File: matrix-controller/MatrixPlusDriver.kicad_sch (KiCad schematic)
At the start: 2 parts, among them IC1 IS31FL3728-QFLS2-TR, U1 1088BS

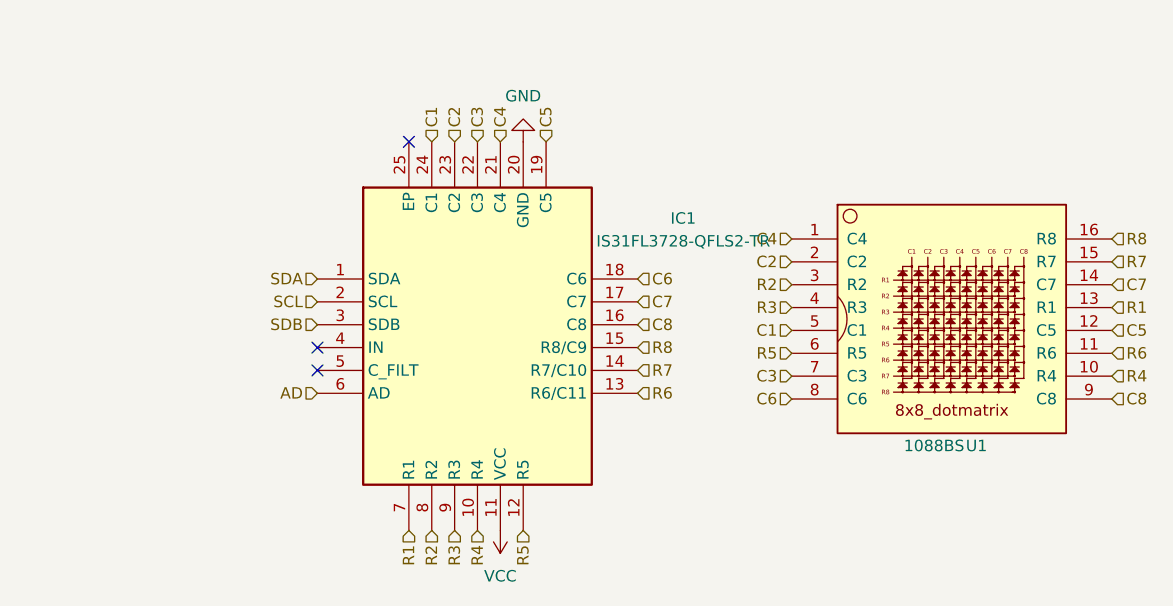
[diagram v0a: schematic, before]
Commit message: Schematic of other pannels mostly completed
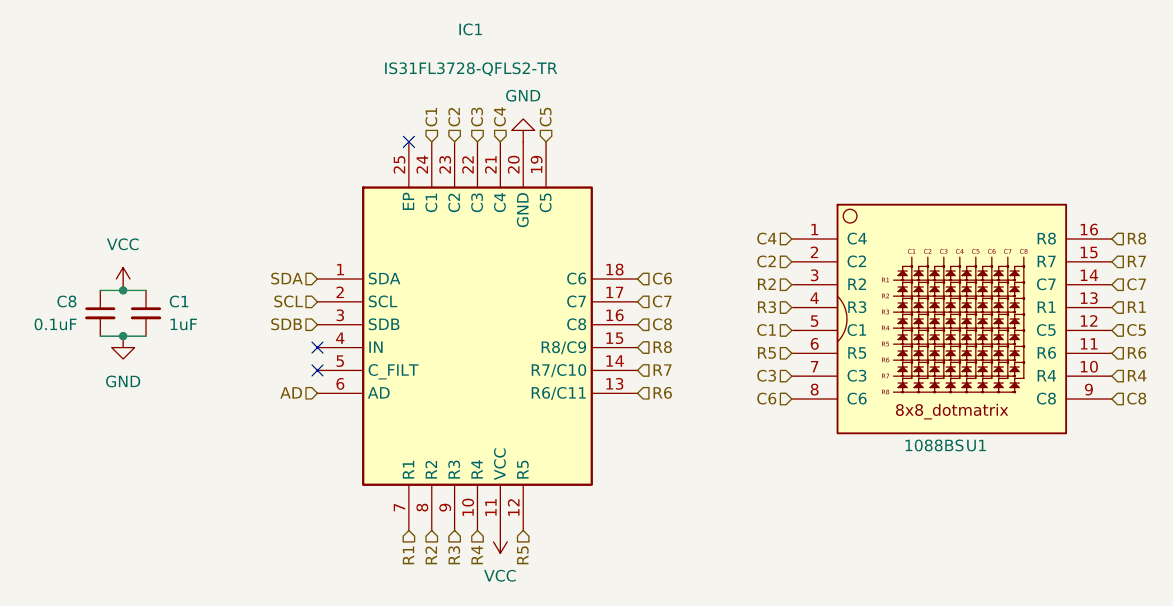
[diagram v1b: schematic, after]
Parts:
- added C1: 1uF, symbol Device:C_Small
- added C8: 0.1uF, symbol Device:C_Small
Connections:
- net GND: now also C1.2, C8.2
- net VCC: now also C1.1, C8.1

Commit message: Updates to pcb. Switched to 4 wire connecions. Added IMU and usb C port footprints
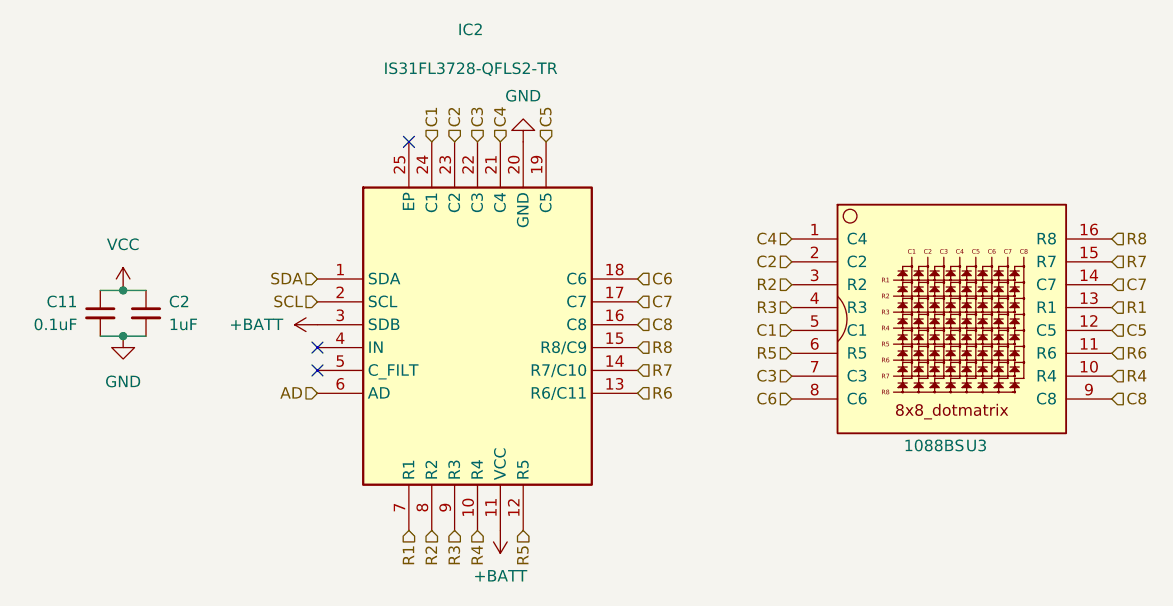
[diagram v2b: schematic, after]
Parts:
- renumbered C8 to C11, C1 to C2, IC1 to IC2, U1 to U3
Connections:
- net VCC: no longer IC2.11 (VCC)
- net SDB renamed +BATT
- net +BATT: now also IC2.11 (VCC)
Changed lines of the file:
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@@
-		)
-	)
-	(hierarchical_label "SDB"
-		(shape input)
-		(at 109.22 60.96 180)
-		(effects
-			(font
-				(size 1.27 1.27)
-			)
-			(justify right)
 		)
 	)
@@
 		(dnp no)
 		(fields_autoplaced yes)
-		(property "Reference" "C1"
+		(property "Reference" "C2"
 			(at 92.71 58.4263 0)
 			(effects
@@
 				(path "/70af459e-5fc9-4c1d-894d-7e71ab2dca95/9d936f13-4432-4cb0-823a-c913cf8ad7e0"
 					(reference "C2")
-					(unit 1)
-				)
-				(path "/70af459e-5fc9-4c1d-894d-7e71ab2dca95/f00320e7-478c-474b-9fd1-c4cf57aa5a54"
-					(reference "C1")
 					(unit 1)
 				)
@@
 		(on_board yes)
 		(dnp no)
-		(property "Reference" "U1"
+		(property "Reference" "U3"
 			(at 183.642 74.422 0)
 			(effects
@@
 				(path "/70af459e-5fc9-4c1d-894d-7e71ab2dca95/9d936f13-4432-4cb0-823a-c913cf8ad7e0"
 					(reference "U3")
-					(unit 1)
-				)
-				(path "/70af459e-5fc9-4c1d-894d-7e71ab2dca95/f00320e7-478c-474b-9fd1-c4cf57aa5a54"
-					(reference "U1")
 					(unit 1)
 				)
@@
 		(on_board yes)
 		(dnp no)
-		(property "Reference" "C8"
+		(property "Reference" "C11"
 			(at 82.55 58.4263 0)
 			(effects
@@
 				(path "/70af459e-5fc9-4c1d-894d-7e71ab2dca95/9d936f13-4432-4cb0-823a-c913cf8ad7e0"
 					(reference "C11")
-					(unit 1)
-				)
-				(path "/70af459e-5fc9-4c1d-894d-7e71ab2dca95/f00320e7-478c-474b-9fd1-c4cf57aa5a54"
-					(reference "C8")
 					(unit 1)
 				)
@@
 		(on_board yes)
 		(dnp no)
-		(property "Reference" "IC1"
+		(property "Reference" "IC2"
 			(at 126.238 28.194 0)
 			(effects
@@
 				(path "/70af459e-5fc9-4c1d-894d-7e71ab2dca95/9d936f13-4432-4cb0-823a-c913cf8ad7e0"
 					(reference "IC2")
-					(unit 1)
-				)
-				(path "/70af459e-5fc9-4c1d-894d-7e71ab2dca95/f00320e7-478c-474b-9fd1-c4cf57aa5a54"
-					(reference "IC1")
 					(unit 1)
 				)
@@
 		(dnp no)
 		(fields_autoplaced yes)
-		(property "Reference" "#PWR033"
+		(property "Reference" "#PWR034"
 			(at 87.63 60.96 0)
 			(effects
@@
 				(path "/70af459e-5fc9-4c1d-894d-7e71ab2dca95/9d936f13-4432-4cb0-823a-c913cf8ad7e0"
 					(reference "#PWR034")
-					(unit 1)
-				)
-				(path "/70af459e-5fc9-4c1d-894d-7e71ab2dca95/f00320e7-478c-474b-9fd1-c4cf57aa5a54"
-					(reference "#PWR033")
 					(unit 1)
 				)
@@
 		(dnp no)
 		(fields_autoplaced yes)
-		(property "Reference" "#PWR053"
+		(property "Reference" "#PWR054"
 			(at 87.63 68.58 0)
 			(effects
@@
 				(path "/70af459e-5fc9-4c1d-894d-7e71ab2dca95/9d936f13-4432-4cb0-823a-c913cf8ad7e0"
 					(reference "#PWR054")
-					(unit 1)
-				)
-				(path "/70af459e-5fc9-4c1d-894d-7e71ab2dca95/f00320e7-478c-474b-9fd1-c4cf57aa5a54"
-					(reference "#PWR053")
-					(unit 1)
-				)
-			)
-		)
-	)
-	(symbol
-		(lib_id "power:VCC")
-		(at 129.54 83.82 180)
-		(unit 1)
-		(exclude_from_sim no)
-		(in_bom yes)
-		(on_board yes)
-		(dnp no)
-		(fields_autoplaced yes)
-		(property "Reference" "#PWR029"
-			(at 129.54 80.01 0)
-			(effects
-				(font
-					(size 1.27 1.27)
-				)
-				(hide yes)
-			)
-		)
-		(property "Value" "VCC"
-			(at 129.54 88.9 0)
-			(effects
-				(font
-					(size 1.27 1.27)
-				)
-			)
-		)
-		(property "Footprint" ""
-			(at 129.54 83.82 0)
-			(effects
-				(font
-					(size 1.27 1.27)
-				)
-				(hide yes)
-			)
-		)
-		(property "Datasheet" ""
-			(at 129.54 83.82 0)
-			(effects
-				(font
-					(size 1.27 1.27)
-				)
-				(hide yes)
-			)
-		)
-		(property "Description" "Power symbol creates a global label with name \"VCC\""
-			(at 129.54 83.82 0)
-			(effects
-				(font
-					(size 1.27 1.27)
-				)
-				(hide yes)
-			)
-		)
-		(pin "1"
-		)
-		(instances
-			(project "matrix-controller"
-				(path "/70af459e-5fc9-4c1d-894d-7e71ab2dca95/1375f33a-57ea-49ee-a7a9-6173eeab9dc4"
-					(reference "#PWR049")
-					(unit 1)
-				)
-				(path "/70af459e-5fc9-4c1d-894d-7e71ab2dca95/20a19834-5d4a-4f9b-97d0-ef4e9cc948c9"
-					(reference "#PWR042")
-					(unit 1)
-				)
-				(path "/70af459e-5fc9-4c1d-894d-7e71ab2dca95/6bcdc057-d713-4dcd-9a4f-906e662a8126"
-					(reference "#PWR035")
-					(unit 1)
-				)
-				(path "/70af459e-5fc9-4c1d-894d-7e71ab2dca95/72834a19-bebc-4ea5-80c1-d8ebc43f143d"
-					(reference "#PWR027")
-					(unit 1)
-				)
-				(path "/70af459e-5fc9-4c1d-894d-7e71ab2dca95/9d936f13-4432-4cb0-823a-c913cf8ad7e0"
-					(reference "#PWR029")
-					(unit 1)
-				)
-				(path "/70af459e-5fc9-4c1d-894d-7e71ab2dca95/f00320e7-478c-474b-9fd1-c4cf57aa5a54"
-					(reference "#PWR029")
 					(unit 1)
 				)
@@
 		(dnp no)
 		(fields_autoplaced yes)
-		(property "Reference" "#PWR01"
+		(property "Reference" "#PWR023"
 			(at 132.08 34.29 0)
 			(effects
@@
 					(unit 1)
 				)
-				(path "/70af459e-5fc9-4c1d-894d-7e71ab2dca95/f00320e7-478c-474b-9fd1-c4cf57aa5a54"
-					(reference "#PWR01")
-					(unit 1)
-				)
+			)
+		)
+	)
+	(symbol
+		(lib_id "power:+BATT")
+		(at 109.22 60.96 90)
+		(unit 1)
+		(exclude_from_sim no)
+		(in_bom yes)
+		(on_board yes)
+		(dnp no)
+		(fields_autoplaced yes)
+		(property "Reference" "#PWR07"
+			(at 113.03 60.96 0)
+			(effects
+				(font
+					(size 1.27 1.27)
+				)
+				(hide yes)
+			)
+		)
+		(property "Value" "+BATT"
+			(at 105.41 60.96 90)
+			(effects
+				(font
+					(size 1.27 1.27)
+				)
+				(justify left)
+			)
+		)
+		(property "Footprint" ""
+			(at 109.22 60.96 0)
+			(effects
+				(font
+					(size 1.27 1.27)
+				)
+				(hide yes)
+			)
+		)
+		(property "Datasheet" ""
+			(at 109.22 60.96 0)
+			(effects
+				(font
+					(size 1.27 1.27)
+				)
+				(hide yes)
+			)
+		)
+		(property "Description" "Power symbol creates a global label with name \"+BATT\""
+			(at 109.22 60.96 0)
+			(effects
+				(font
+					(size 1.27 1.27)
+				)
+				(hide yes)
+			)
+		)
+		(pin "1"
+		)
+		(instances
+			(project ""
+				(path "/70af459e-5fc9-4c1d-894d-7e71ab2dca95/1375f33a-57ea-49ee-a7a9-6173eeab9dc4"
+					(reference "#PWR033")
+					(unit 1)
+				)
+				(path "/70af459e-5fc9-4c1d-894d-7e71ab2dca95/20a19834-5d4a-4f9b-97d0-ef4e9cc948c9"
+					(reference "#PWR029")
+					(unit 1)
+				)
+				(path "/70af459e-5fc9-4c1d-894d-7e71ab2dca95/6bcdc057-d713-4dcd-9a4f-906e662a8126"
+					(reference "#PWR028")
+					(unit 1)
+				)
+				(path "/70af459e-5fc9-4c1d-894d-7e71ab2dca95/72834a19-bebc-4ea5-80c1-d8ebc43f143d"
+					(reference "#PWR027")
+					(unit 1)
+				)
+				(path "/70af459e-5fc9-4c1d-894d-7e71ab2dca95/9d936f13-4432-4cb0-823a-c913cf8ad7e0"
+					(reference "#PWR07")
+					(unit 1)
+				)
+			)
+		)
+	)
+	(symbol
+		(lib_id "power:+BATT")
+		(at 129.54 83.82 180)
+		(unit 1)
+		(exclude_from_sim no)
+		(in_bom yes)
+		(on_board yes)
+		(dnp no)
+		(fields_autoplaced yes)
+		(property "Reference" "#PWR035"
+			(at 129.54 80.01 0)
+			(effects
+				(font
+					(size 1.27 1.27)
+				)
+				(hide yes)
+			)
+		)
+		(property "Value" "+BATT"
+			(at 129.54 88.9 0)
+			(effects
+				(font
+					(size 1.27 1.27)
+				)
+			)
+		)
+		(property "Footprint" ""
+			(at 129.54 83.82 0)
+			(effects
+				(font
+					(size 1.27 1.27)
+				)
+				(hide yes)
+			)
+		)
+		(property "Datasheet" ""
+			(at 129.54 83.82 0)
+			(effects
+				(font
+					(size 1.27 1.27)
+				)
+				(hide yes)
+			)
+		)
+		(property "Description" "Power symbol creates a global label with name \"+BATT\""
+			(at 129.54 83.82 0)
+			(effects
+				(font
+					(size 1.27 1.27)
+				)
+				(hide yes)
+			)
+		)
+		(pin "1"
+		)
+		(instances
+			(project "matrix-controller"
+				(path "/70af459e-5fc9-4c1d-894d-7e71ab2dca95/1375f33a-57ea-49ee-a7a9-6173eeab9dc4"
+					(reference "#PWR053")
+					(unit 1)
+				)
+				(path "/70af459e-5fc9-4c1d-894d-7e71ab2dca95/20a19834-5d4a-4f9b-97d0-ef4e9cc948c9"
+					(reference "#PWR049")
+					(unit 1)
+				)
+				(path "/70af459e-5fc9-4c1d-894d-7e71ab2dca95/6bcdc057-d713-4dcd-9a4f-906e662a8126"
+					(reference "#PWR044")
+					(unit 1)
+				)
+				(path "/70af459e-5fc9-4c1d-894d-7e71ab2dca95/72834a19-bebc-4ea5-80c1-d8ebc43f143d"
+					(reference "#PWR042")
+					(unit 1)
+				)
+				(path "/70af459e-5fc9-4c1d-894d-7e71ab2dca95/9d936f13-4432-4cb0-823a-c913cf8ad7e0"
+					(reference "#PWR035")
+					(unit 1)
+				)
